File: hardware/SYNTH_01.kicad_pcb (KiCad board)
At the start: 2 copper layers, 112.7 x 150 mm, 100 parts, among them J2 Conn_01x04_Pin, SW1 SW_Push_45deg, SW10 SW_Push_45deg, SW11 SW_Push_45deg, SW12 SW_Push_45deg, SW13 SW_Push_45deg, SW14 SW_Push_45deg, SW15 SW_Push_45deg, SW16 SW_Push_45deg, SW17 SW_Push_45deg, SW18 SW_Push_45deg, SW19 SW_Push_45deg, SW2 SW_Push_45deg, SW20 SW_Push_45deg, SW21 SW_Push_45deg, SW3 SW_Push_45deg, SW4 SW_Push_45deg, SW5 SW_Push_45deg, SW6 SW_Push_45deg, SW7 SW_Push_45deg, SW8 SW_Push_45deg, SW9 SW_Push_45deg, U1 MCP23017-E/SP, U2 74AHCT1G125

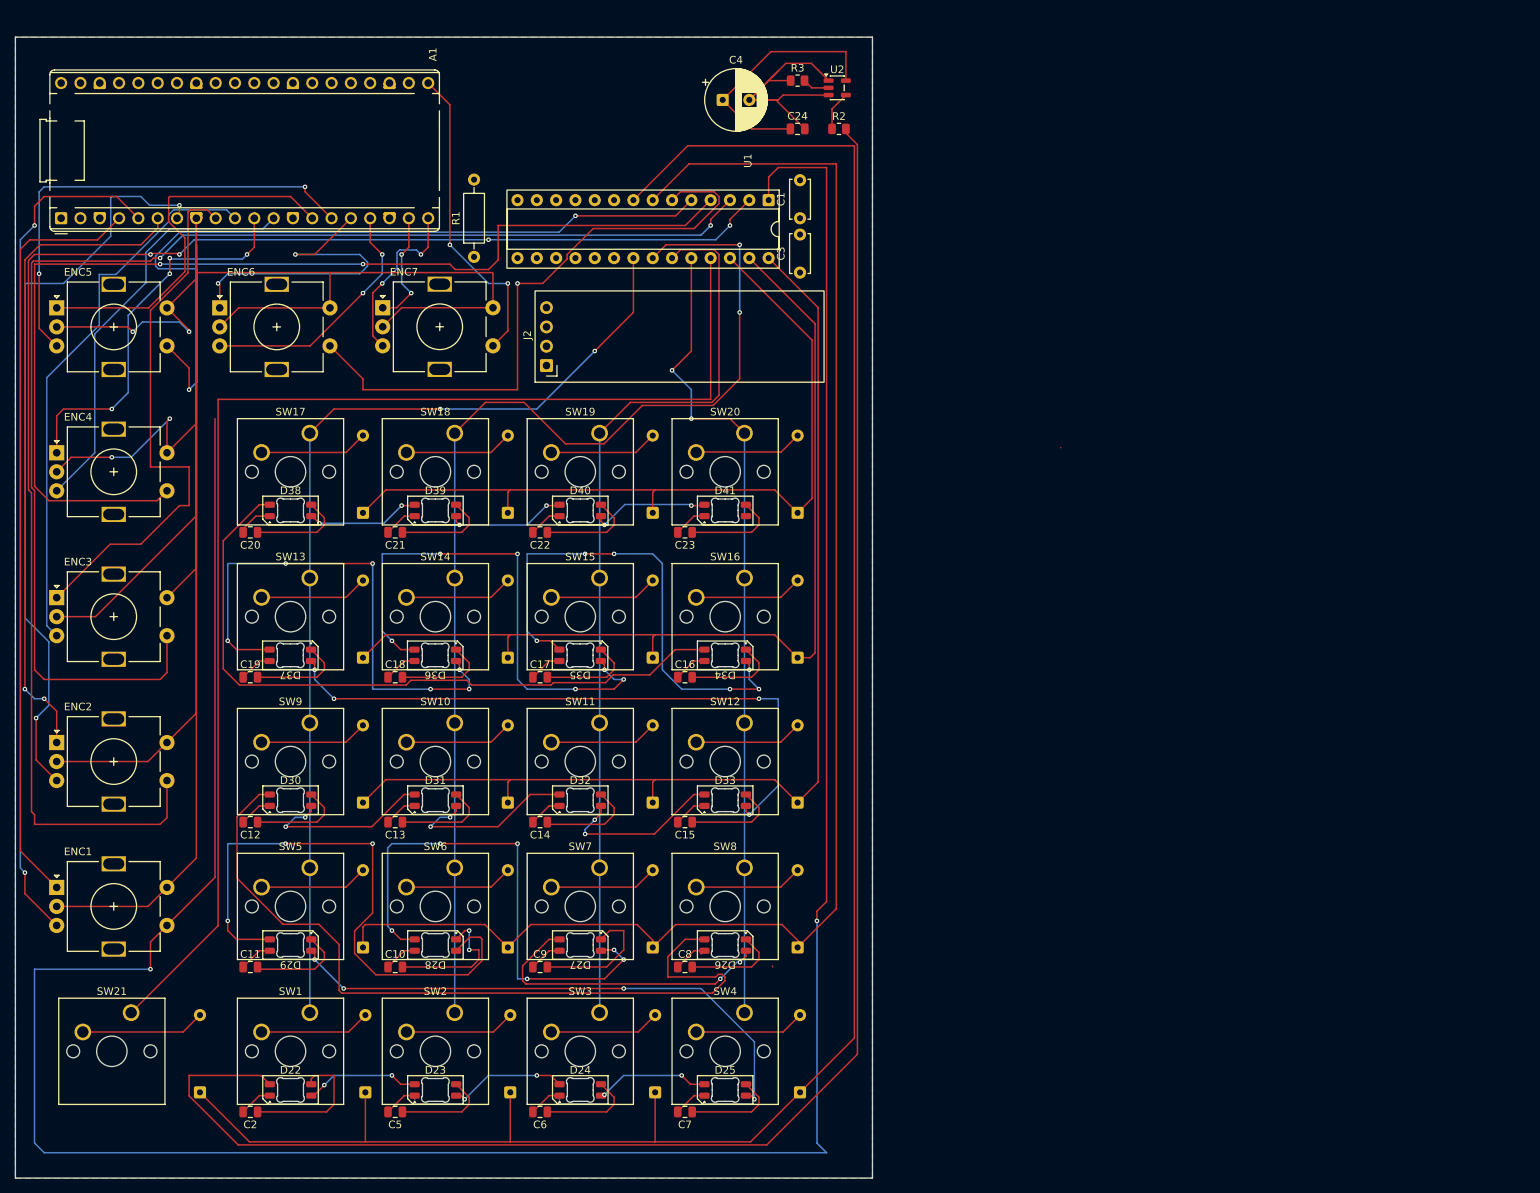
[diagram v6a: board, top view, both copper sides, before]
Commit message: PCB REFACTOR: connecting all leds to ground
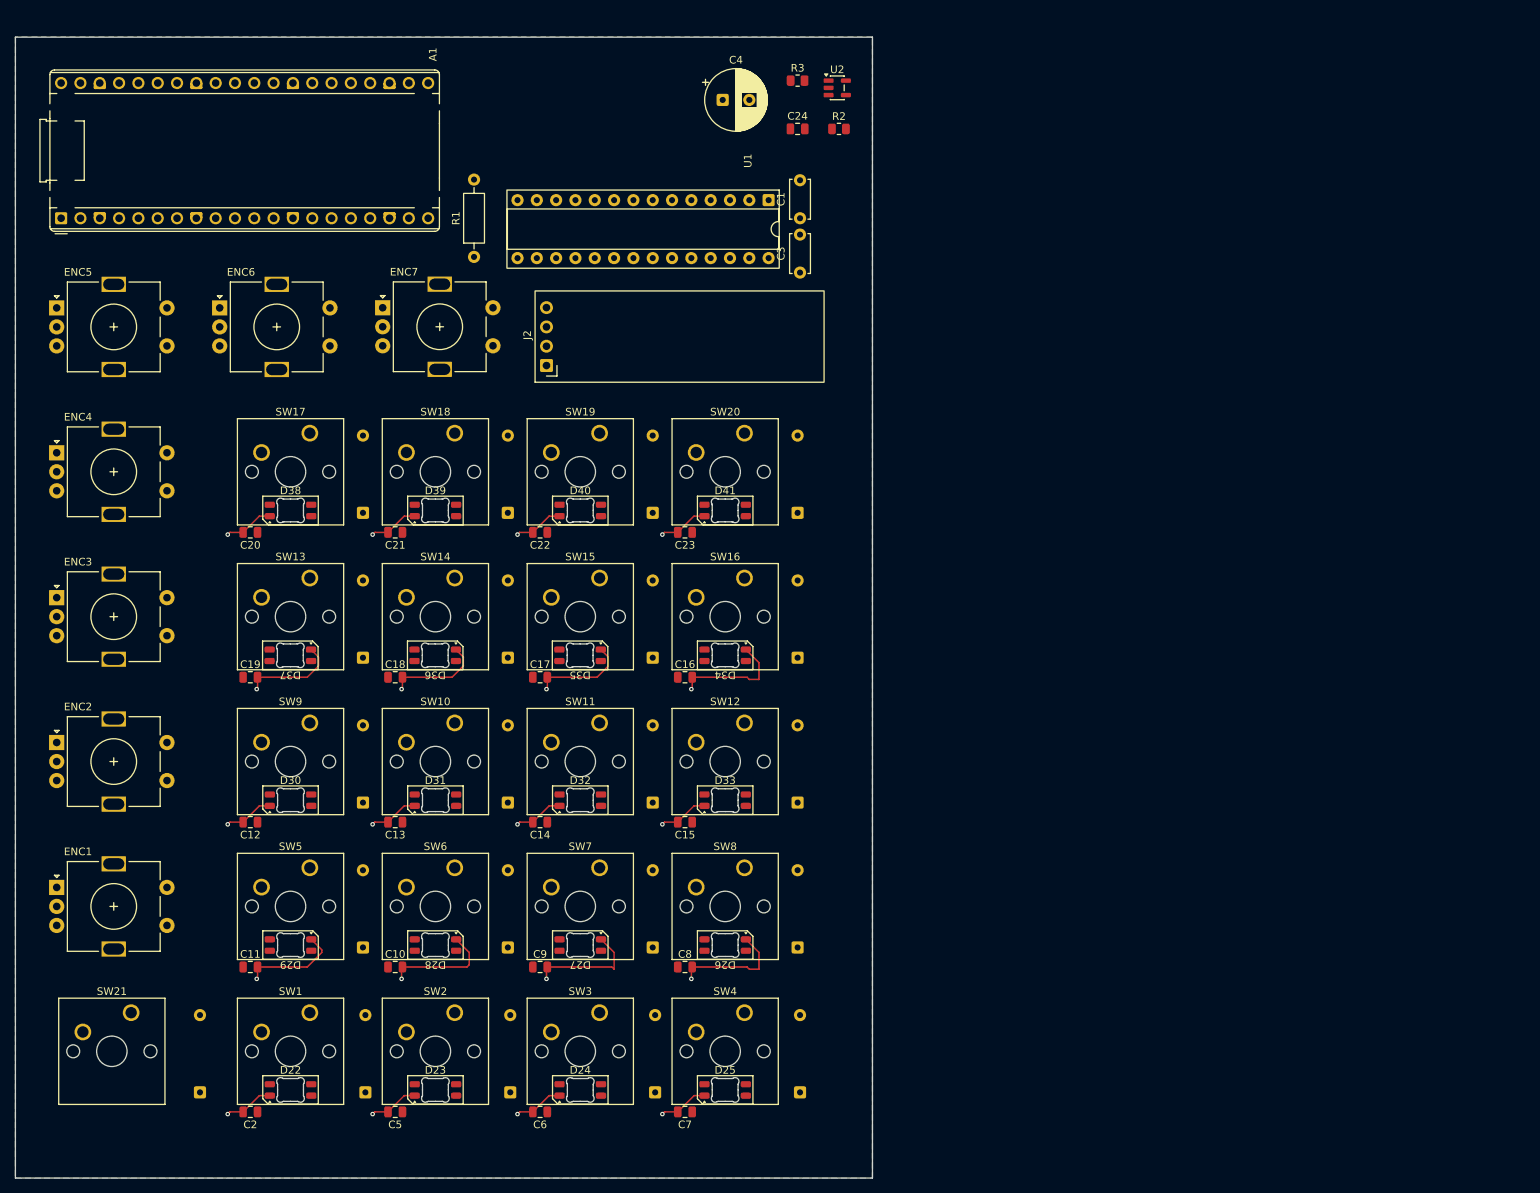
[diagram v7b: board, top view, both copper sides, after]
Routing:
- net GND: track 668.3 -> 189.9 mm, vias 6 -> 20
- net /SYNTH_01/E1_SW: track 360.4 -> 0.00 mm, vias 2 -> 0
- net /SYNTH_01/ROW4: track 263.2 -> 0.00 mm
- net Net-(D22-DIN): track 231.6 -> 0.00 mm
- net LED_5V: track 225.6 -> 0.00 mm
- net /SYNTH_01/ROW3: track 198.8 -> 0.00 mm
- net /SYNTH_01/E2_SW: track 195.7 -> 0.00 mm, vias 5 -> 0
- net /SYNTH_01/E3_SW: track 172.6 -> 0.00 mm, vias 2 -> 0
- net /SYNTH_01/COL_SHIFT: track 168.7 -> 0.00 mm
- net /SYNTH_01/COL1: track 150.9 -> 0.00 mm, vias 2 -> 0
- net /SYNTH_01/E4_SW: track 143.6 -> 0.00 mm, vias 2 -> 0
- net /SYNTH_01/ROW2: track 141.4 -> 0.00 mm
- net /SYNTH_01/COL0: track 132.5 -> 0.00 mm, vias 2 -> 0
- net /SYNTH_01/ROW1: track 124.0 -> 0.00 mm
- net /SYNTH_01/COL2: track 119.4 -> 0.00 mm
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
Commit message: PCB REFACTOR: new LEDs connections are working
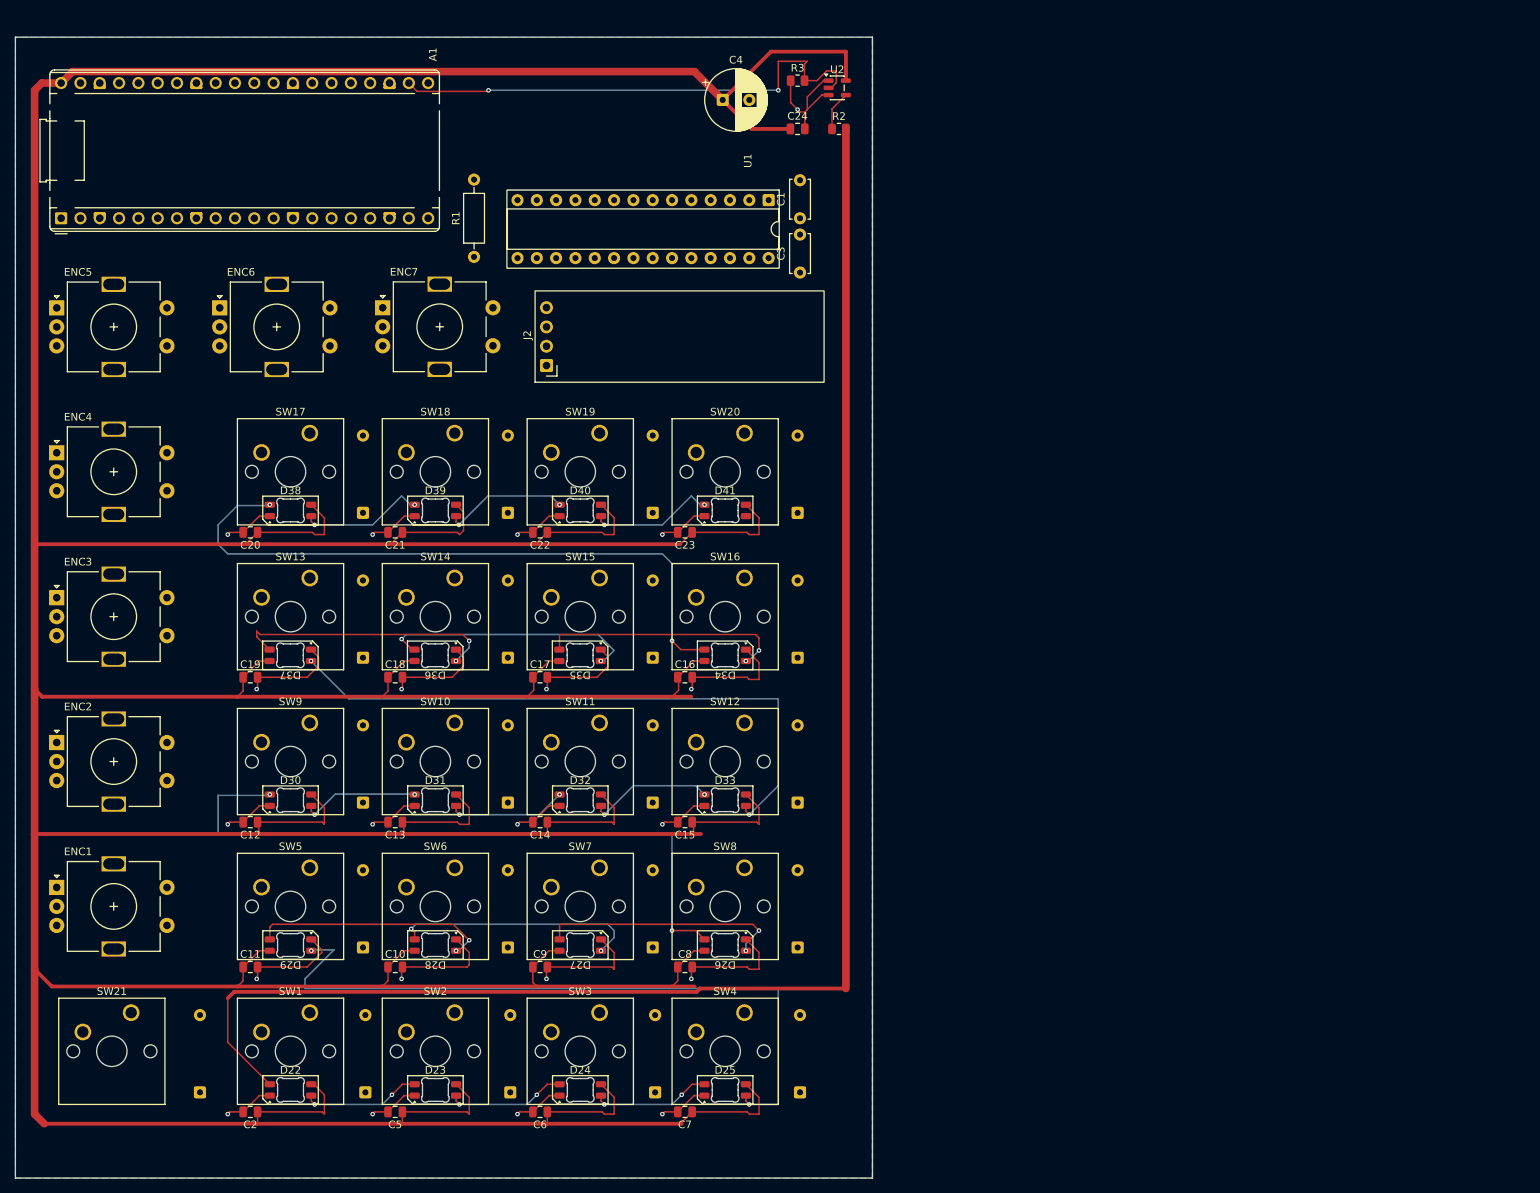
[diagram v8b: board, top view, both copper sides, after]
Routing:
- net LED_5V: track 0.00 -> 935.5 mm
- net Net-(D22-DIN): track 0.00 -> 208.5 mm
- net Net-(D25-DOUT): track 0.00 -> 92.3 mm, vias 0 -> 2
- net Net-(D26-DOUT): track 0.00 -> 89.1 mm, vias 0 -> 2
- net Net-(D34-DOUT): track 0.00 -> 86.1 mm, vias 0 -> 2
- net Net-(D33-DOUT): track 0.00 -> 81.7 mm, vias 0 -> 2
- net LED_DATA: track 0.00 -> 66.9 mm, vias 0 -> 2
- net Net-(D36-DIN): track 0.00 -> 35.0 mm, vias 0 -> 2
- net Net-(D35-DIN): track 0.00 -> 33.6 mm, vias 0 -> 2
- net Net-(D34-DIN): track 0.00 -> 32.3 mm, vias 0 -> 2
- net Net-(D27-DIN): track 0.00 -> 32.2 mm, vias 0 -> 2
- net Net-(D26-DIN): track 0.00 -> 31.9 mm, vias 0 -> 2
- net Net-(D28-DIN): track 0.00 -> 31.1 mm, vias 0 -> 2
- net GND: track 189.9 -> 206.8 mm, vias 20 -> 21
- net Net-(D39-DOUT): track 0.00 -> 16.6 mm, vias 0 -> 2
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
